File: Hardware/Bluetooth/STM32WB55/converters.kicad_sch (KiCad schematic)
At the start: 21 parts, among them IC2 MP1475SGJ-P, U5 BU33SD5WG-TR

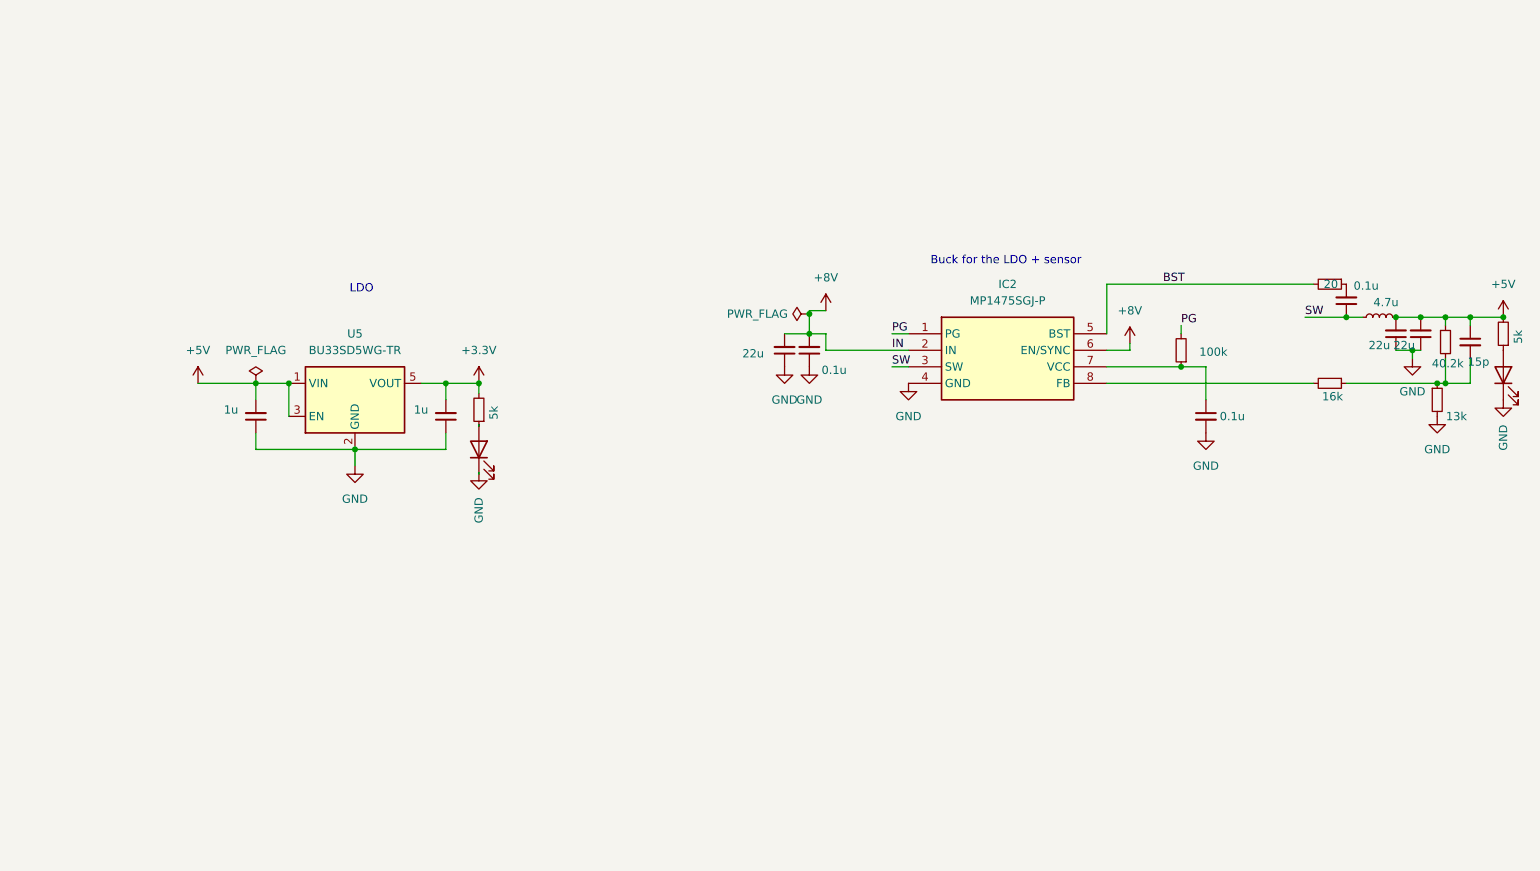
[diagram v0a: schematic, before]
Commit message: schematic update
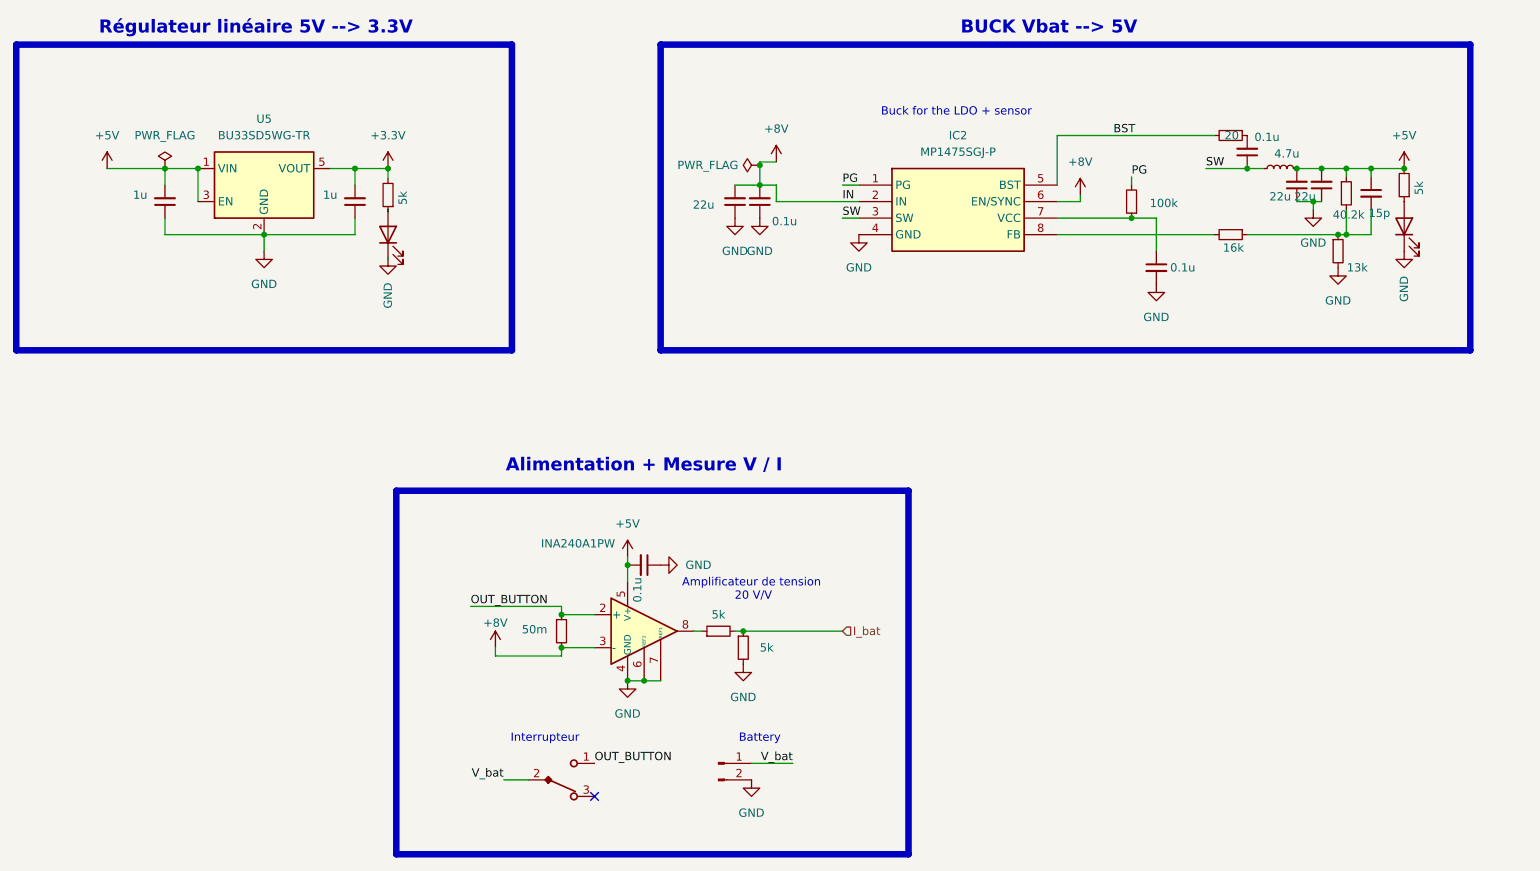
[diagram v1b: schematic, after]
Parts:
- added C35: 0.1u, Capacitor_SMD:C_0603_1608Metric, symbol Device:C_Small
- added J9: Conn_01x02_Pin, Connector_JST:JST_XH_B2B-XH-A_1x02_P2.50mm_Vertical, symbol Connector:Conn_01x02_Pin
- added R15: 50m, Resistor_SMD:R_6431, symbol Device:R_Small
- added R16, R17: 5k, Resistor_SMD:R_0603_1608Metric, symbol Device:R_Small
- added SW1: SW_Wurth, Button_Switch_THT:SW_Wurth_WS-TOTV_472121020311, symbol Switch:SW_Wurth
- added U2: INA240A1PW, Package_SO:TSSOP-8_4.4x3mm_P0.65mm, symbol Amplifier_Current:INA240A1PW
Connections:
- net +5V: now also C35.2, U2.5 (V+)
- net +8V: now also R15.2, U2.3 (-)
- net GND: now also C35.1, J9.2 (Pin_2), R16.2, U2.1 (GND), U2.4 (GND), U2.6 (REF2), U2.7 (REF1)
- new net: R17.1, U2.8
- new net I_bat: R16.1, R17.2
- new net OUT_BUTTON: R15.1, SW1.1, U2.2 (+)
- new net V_bat: J9.1 (Pin_1), SW1.2
- no-connect marks 0 -> 1
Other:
- note added: "Alimentation + Mesure V / I"
- note added: "Amplificateur de tension 20 V/V"
- note added: "BUCK Vbat --> 5V"
- note added: "Battery"
- note added: "Interrupteur"
- note added: "Régulateur linéaire 5V --> 3.3V"
- note removed: "LDO"
- moved on the sheet: IC2, U5
